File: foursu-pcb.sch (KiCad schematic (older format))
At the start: 24 parts, among them SW1 SW_Push, U1 ATmega32U4-AU, Y1 16MHz

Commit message: uh yes microcontroller stuff
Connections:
- net COL0: now also U1.29 (PB5)
- net COL1: now also U1.30 (PB6)
- net GND: now also C2.2, C3.2
- net ROW0: now also U1.27 (PD7)
- net ROW1: now also U1.28 (PB4)
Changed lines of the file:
@@
 Text GLabel 5300 4500 0    50   Input ~ 0
 ROW1
+Wire Wire Line
+	1700 2750 1700 2900
+Connection ~ 1700 2750
+Connection ~ 1700 2900
+Wire Wire Line
+	3750 2800 3850 2800
+Wire Wire Line
+	3850 2700 3750 2700
+Text GLabel 3850 2800 2    50   Input ~ 0
+COL0
+Text GLabel 3850 2900 2    50   Input ~ 0
+COL1
+Text GLabel 3850 2700 2    50   Input ~ 0
+ROW1
+Text GLabel 3850 4200 2    50   Input ~ 0
+ROW0
+Wire Wire Line
+	3850 2900 3750 2900
+Wire Wire Line
+	3750 4200 3850 4200
 $EndSCHEMATC

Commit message: finished first prototype?
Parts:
- removed C1, C5, C6: 0.1uF, Capacitor_SMD:C_0805_2012Metric, symbol Device:C_Small
- removed C2, C3: 22pF, Capacitor_SMD:C_0805_2012Metric, symbol Device:C_Small
- removed C4: 1uF, Capacitor_SMD:C_0805_2012Metric, symbol Device:C_Small
- removed C7: 10uF, Capacitor_SMD:C_0805_2012Metric, symbol Device:C_Small
- removed D1, D2, D3, D4: SOD-123, Diode_SMD:D_SOD-123, symbol Device:D_Small
- removed F1: Polyfuse, Fuse:Fuse_1206_3216Metric, symbol Device:Polyfuse
- removed R1, R2: 22, Resistor_SMD:R_0805_2012Metric, symbol Device:R_Small
- removed R3, R4: 10k, Resistor_SMD:R_0805_2012Metric, symbol Device:R_Small
- removed SW1: SW_Push, random-keyboard-parts:SKQG-1155865, symbol Switch:SW_Push
- removed U1: ATmega32U4-AU, Package_QFP:TQFP-44_10x10mm_P0.8mm, symbol MCU_Microchip_ATmega:ATmega32U4-AU
- removed USB1: Molex-0548190519, random-keyboard-parts:Molex-0548190589, symbol random-keyboard-parts:Molex-0548190519
- removed Y1: 16MHz, Crystal:Crystal_SMD_3225-4Pin_3.2x2.5mm, symbol Device:Crystal_GND24_Small
- added B1: SPARKFUN_PRO_MICRO, Boards:SPARKFUN_PRO_MICRO, symbol SparkFun-Boards:SPARKFUN_PRO_MICRO
- added D1, D2, D3, D4, D5: 1N4148, Diode_THT:D_DO-35_SOD27_P7.62mm_Horizontal, symbol Diode:1N4148
- added SW1: Rotary_Encoder_Switch, Rotary_Encoder:RotaryEncoder_Alps_EC11E-Switch_Vertical_H20mm, symbol Device:Rotary_Encoder_Switch
- MX1, MX2, MX3, MX4: value MX-NoLED -> MX-LED
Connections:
- net labels added: COL2, COL3, COL4, ENC0, ENC1
- net labels removed: +5V, D+, D-, ROW1, VCC
- wire segments 65 -> 21

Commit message: files for initial prototype
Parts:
- MX1, MX2, MX3, MX4: footprint MX_Alps_Hybrid:MX-1U-NoLED -> MX_Only:MXOnly-1U-NoLED
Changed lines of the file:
@@
 F 0 "MX1" H 5983 3673 60  0000 C CNN
 F 1 "MX-LED" H 5983 3599 20  0000 C CNN
-F 2 "MX_Alps_Hybrid:MX-1U-NoLED" H 5325 3425 60  0001 C CNN
+F 2 "MX_Only:MXOnly-1U-NoLED" H 5325 3425 60  0001 C CNN
 F 3 "" H 5325 3425 60  0001 C CNN
 	1    5950 3450
@@
 F 0 "MX2" H 6583 3673 60  0000 C CNN
 F 1 "MX-LED" H 6583 3599 20  0000 C CNN
-F 2 "MX_Alps_Hybrid:MX-1U-NoLED" H 5925 3425 60  0001 C CNN
+F 2 "MX_Only:MXOnly-1U-NoLED" H 5925 3425 60  0001 C CNN
 F 3 "" H 5925 3425 60  0001 C CNN
 	1    6550 3450
@@
 F 0 "MX3" H 7233 3673 60  0000 C CNN
 F 1 "MX-LED" H 7233 3599 20  0000 C CNN
-F 2 "MX_Alps_Hybrid:MX-1U-NoLED" H 6575 3425 60  0001 C CNN
+F 2 "MX_Only:MXOnly-1U-NoLED" H 6575 3425 60  0001 C CNN
 F 3 "" H 6575 3425 60  0001 C CNN
 	1    7200 3450
@@
 F 0 "MX4" H 7933 3673 60  0000 C CNN
 F 1 "MX-LED" H 7933 3599 20  0000 C CNN
-F 2 "MX_Alps_Hybrid:MX-1U-NoLED" H 7275 3425 60  0001 C CNN
+F 2 "MX_Only:MXOnly-1U-NoLED" H 7275 3425 60  0001 C CNN
 F 3 "" H 7275 3425 60  0001 C CNN
 	1    7900 3450

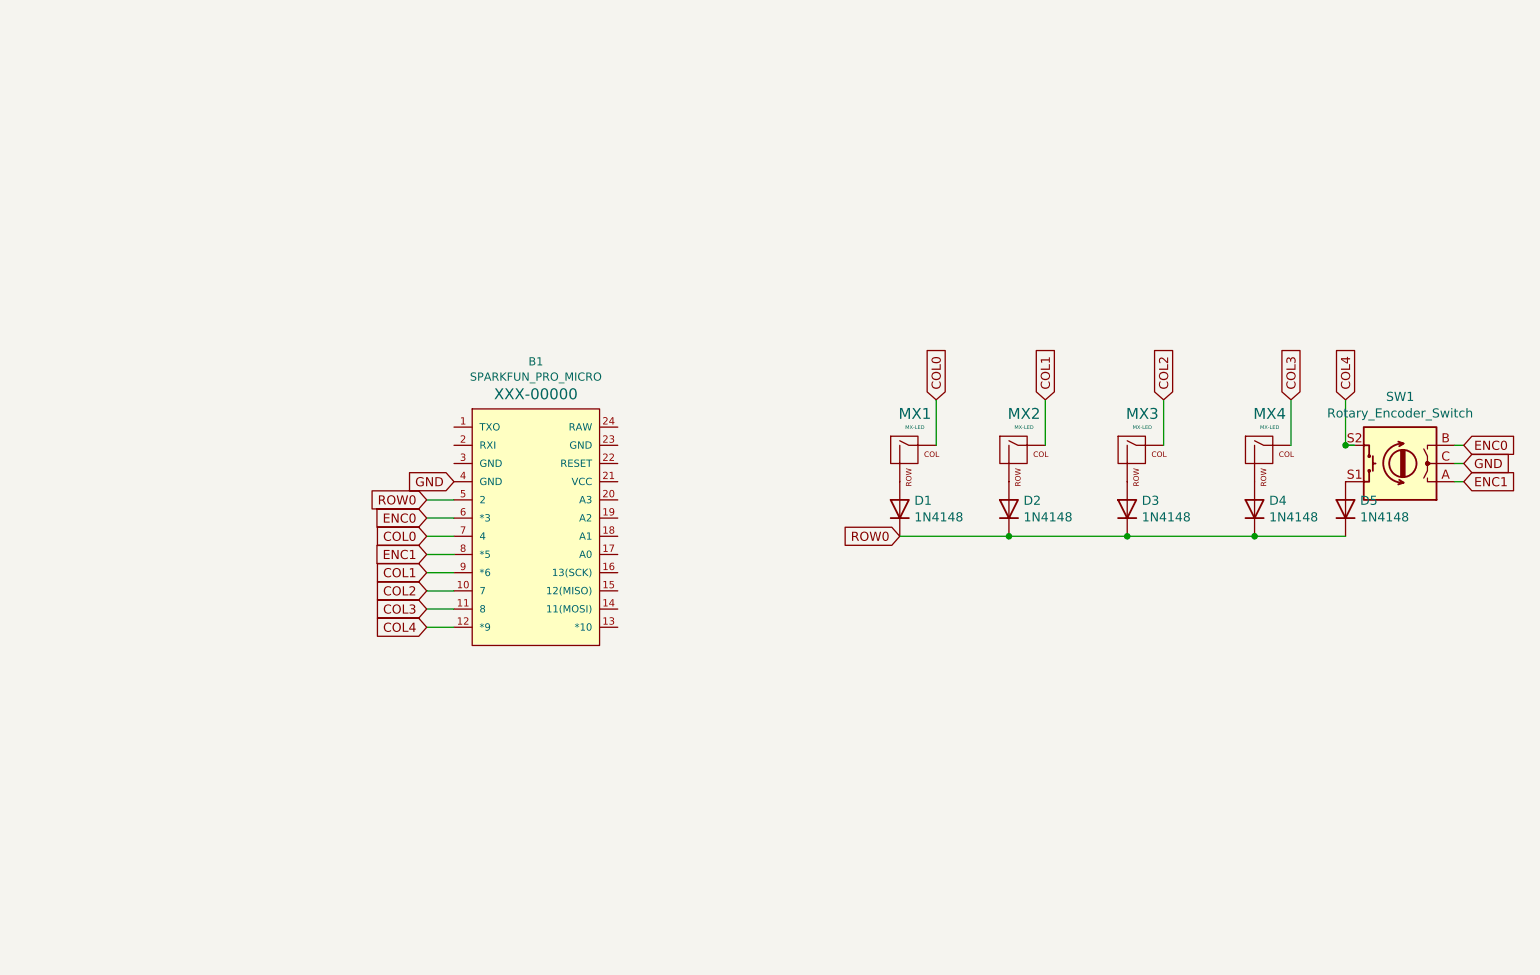
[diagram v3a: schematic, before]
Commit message: finished pcb routing
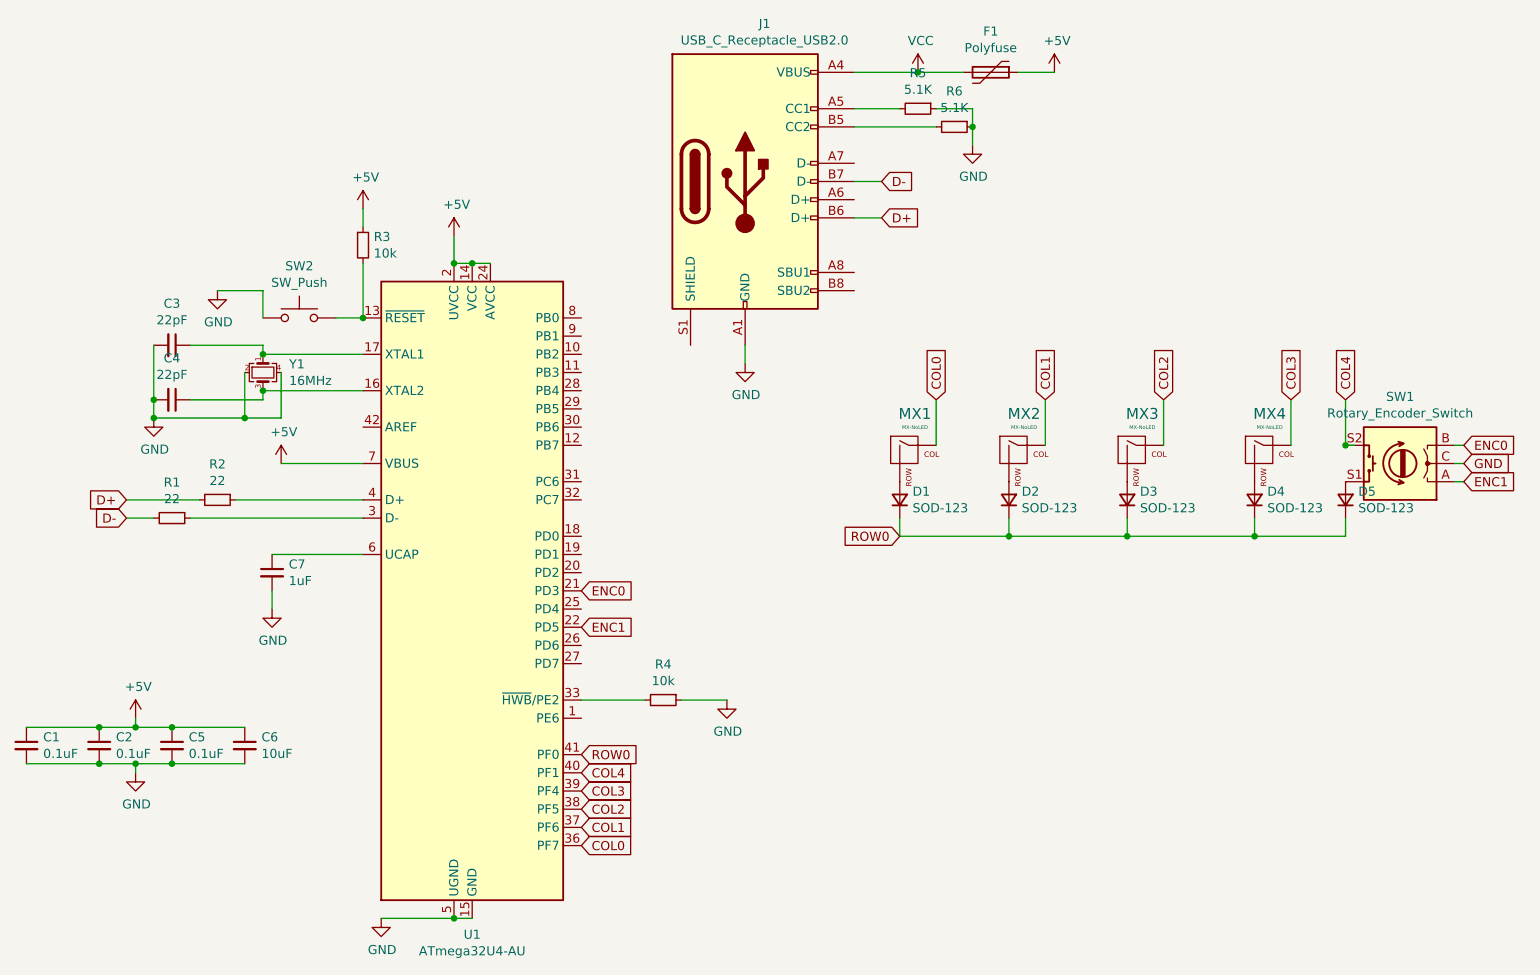
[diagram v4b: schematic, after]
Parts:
- removed B1: SPARKFUN_PRO_MICRO, Boards:SPARKFUN_PRO_MICRO, symbol SparkFun-Boards:SPARKFUN_PRO_MICRO
- removed D1, D2, D3, D4, D5: 1N4148, Diode_THT:D_DO-35_SOD27_P7.62mm_Horizontal, symbol Diode:1N4148
- added C1, C2, C5: 0.1uF, Capacitor_SMD:C_0805_2012Metric, symbol Device:C_Small
- added C3, C4: 22pF, Capacitor_SMD:C_0805_2012Metric, symbol Device:C_Small
- added C6: 10uF, Capacitor_SMD:C_0805_2012Metric, symbol Device:C_Small
- added C7: 1uF, Capacitor_SMD:C_0805_2012Metric, symbol Device:C_Small
- added D1, D2, D3, D4, D5: SOD-123, Diode_SMD:D_SOD-123, symbol Device:D_Small
- added F1: Polyfuse, Fuse:Fuse_1206_3216Metric, symbol Device:Polyfuse
- added J1: USB_C_Receptacle_USB2.0, Connector_USB:USB_C_Receptacle_Amphenol_12401548E4-2A, symbol Connector:USB_C_Receptacle_USB2.0
- added R1, R2: 22, Resistor_SMD:R_0805_2012Metric, symbol Device:R_Small
- added R3, R4: 10k, Resistor_SMD:R_0805_2012Metric, symbol Device:R_Small
- added R5, R6: 5.1K, Resistor_SMD:R_0805_2012Metric, symbol Device:R_Small
- added SW2: SW_Push, random-keyboard-parts:SKQG-1155865, symbol Switch:SW_Push
- added U1: ATmega32U4-AU, Package_QFP:TQFP-44_10x10mm_P0.8mm, symbol MCU_Microchip_ATmega:ATmega32U4-AU
- added Y1: 16MHz, Crystal:Crystal_SMD_3225-4Pin_3.2x2.5mm, symbol Device:Crystal_GND24_Small
- MX1, MX2, MX3, MX4: value MX-LED -> MX-NoLED; footprint MX_Only:MXOnly-1U-NoLED -> MX_Alps_Hybrid:MX-1U-NoLED
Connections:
- net labels added: +5V, D+, D-, VCC
- wire segments 21 -> 70
